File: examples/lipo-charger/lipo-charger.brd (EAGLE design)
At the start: 36 x 12 mm, 10 parts, among them IC2 LIPO_CHARGER/OT

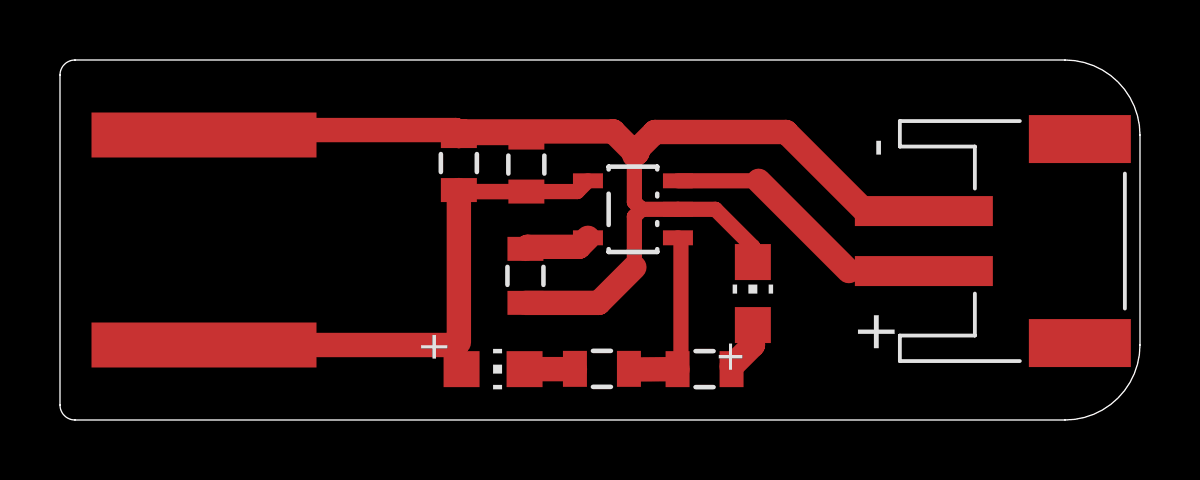
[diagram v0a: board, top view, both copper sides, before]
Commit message: lipo board uses new parts
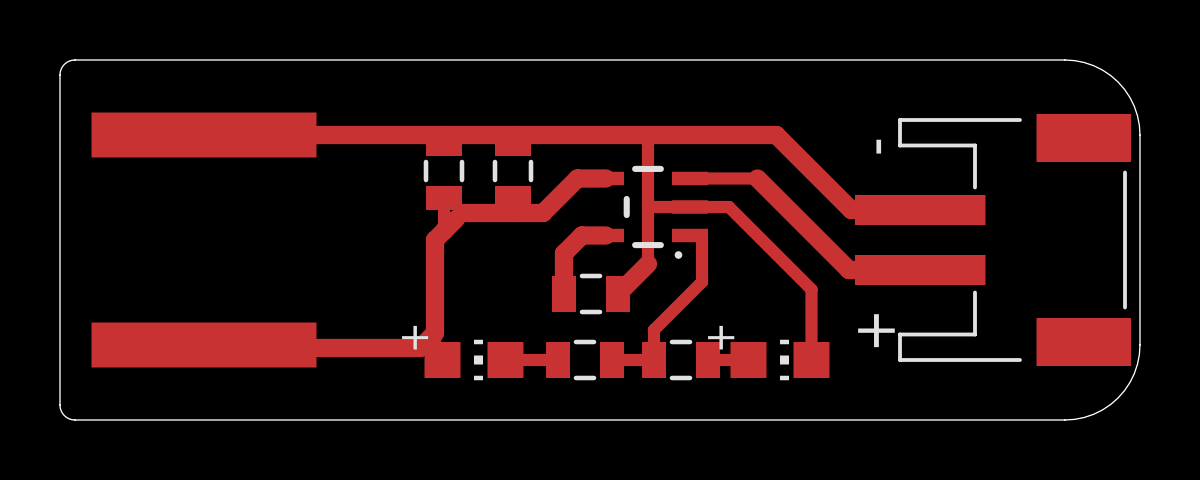
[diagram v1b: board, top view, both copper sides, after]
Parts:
- removed CN1: (no value), homemade-hardware:JST-PH-2-SMT-RA
- removed IC2: LIPO_CHARGER/OT, homemade-hardware:SOT23-5L
- added IC1: IC_LIPO_CHARGER, homemade-hardware:SOT23-5
- added U$1: CONN_BATTERY-LIPO-HORIZ, homemade-hardware:JST-PH-2-SMT-RA
- LED1: value RED-2V/20mA -> Red
- LED2: value GREEN-2V/20mA -> Blue
- R1: value 10k -> 150
- R3: value 150 -> 10k
- U$2: value USB-PCB-POWER -> CONN_USB_PCB_POWER; device homemade-hardware:USB-A-PCB-POWER -> homemade-hardware:USB-PCB-POWER
- moved R3 4.54 mm to (17.7, 4.20)
- moved R1 3.44 mm to (17.5, 2.00), turned to 180 degrees
- moved R2 2.65 mm to (20.7, 2.00)
- moved LED2 2.39 mm to (24.0, 2.00), turned to 270 degrees
- moved LED1 0.70 mm to (13.8, 2.00)
- moved C1 0.56 mm to (12.8, 8.30)
- moved C2 0.49 mm to (15.1, 8.30)
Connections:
- net 5V: now also IC1.4; no longer IC2.4
- net BATTERY: now also IC1.3, U$1.1; no longer CN1.1, IC2.3
- net CURRENT-CONTROL: now also IC1.5, R3.2; no longer IC2.5, R1.2
- net GND: now also IC1.2, R3.1, U$1.2; no longer CN1.2, IC2.2, R1.1
- net N$2: now also R1.2; no longer R2.2
- net N$3: now also R2.1; no longer R3.1
- net STATUS: now also IC1.1, R1.1, R2.2; no longer IC2.1, R2.1, R3.2
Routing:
- net 5V: track 21.3 -> 20.2 mm
- net GND: track 41.2 -> 40.2 mm
- net CURRENT-CONTROL: track 2.24 -> 3.00 mm
- net STATUS: track 6.09 -> 6.61 mm
- net BATTERY: track 9.44 -> 8.94 mm

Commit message: finishes lipo pcb design
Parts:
- moved C1 0.90 mm to (13.7, 8.30)
- moved LED2 0.60 mm to (24.6, 2.00)
- moved C2 0.50 mm to (15.6, 8.30)
- moved R2 0.20 mm to (20.9, 2.00)
- moved R3 0.20 mm to (17.5, 4.20)
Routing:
- net 5V: track 20.2 -> 19.7 mm
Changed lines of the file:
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@@
 <element name="U$2" library="homemade-hardware" package="USB-PCB-POWER" value="CONN_USB_PCB_POWER" x="5" y="6" smashed="yes"/>
 <element name="LED1" library="homemade-hardware" package="CHIP-LED0805" value="Red" x="13.8" y="2" smashed="yes" rot="R270"/>
-<element name="LED2" library="homemade-hardware" package="CHIP-LED0805" value="Blue" x="24" y="2" smashed="yes" rot="R270"/>
-<element name="C1" library="homemade-hardware" package="0805" value="10uF" x="12.8" y="8.3" smashed="yes" rot="R90"/>
-<element name="C2" library="homemade-hardware" package="0805" value="0.1uF" x="15.1" y="8.3" smashed="yes" rot="R90"/>
-<element name="R2" library="homemade-hardware" package="0805" value="150" x="20.7" y="2" smashed="yes" rot="R180"/>
+<element name="LED2" library="homemade-hardware" package="CHIP-LED0805" value="Blue" x="24.6" y="2" smashed="yes" rot="R270"/>
+<element name="C1" library="homemade-hardware" package="0805" value="10uF" x="13.7" y="8.3" smashed="yes" rot="R90"/>
+<element name="C2" library="homemade-hardware" package="0805" value="0.1uF" x="15.6" y="8.3" smashed="yes" rot="R90"/>
+<element name="R2" library="homemade-hardware" package="0805" value="150" x="20.9" y="2" smashed="yes" rot="R180"/>
 <element name="R1" library="homemade-hardware" package="0805" value="150" x="17.5" y="2" smashed="yes" rot="R180"/>
-<element name="R3" library="homemade-hardware" package="0805" value="10k" x="17.7" y="4.2" smashed="yes" rot="R180"/>
+<element name="R3" library="homemade-hardware" package="0805" value="10k" x="17.5" y="4.2" smashed="yes" rot="R180"/>
 </elements>
 <signals>
@@
 <contactref element="IC1" pad="3"/>
 <contactref element="U$1" pad="1"/>
-<wire x1="21.0001" y1="8.05" x2="23.25" y2="8.05" width="0.4064" layer="1"/>
-<wire x1="23.25" y1="8.05" x2="26.3" y2="5" width="0.6096" layer="1"/>
+<wire x1="23.3001" y1="7.95" x2="23.2001" y2="8.05" width="0.4064" layer="1"/>
+<wire x1="21.0001" y1="8.05" x2="23.2001" y2="8.05" width="0.4064" layer="1"/>
+<wire x1="23.35" y1="7.95" x2="23.3001" y2="7.95" width="0.4064" layer="1"/>
+<wire x1="23.35" y1="7.95" x2="26.3" y2="5" width="0.6096" layer="1"/>
 <wire x1="26.3" y1="5" x2="28.675" y2="5" width="0.6096" layer="1"/>
 </signal>
@@
 <contactref element="IC1" pad="5"/>
 <contactref element="R3" pad="2"/>
-<wire x1="16.8" y1="4.2" x2="16.8" y2="5.5501" width="0.6096" layer="1"/>
-<wire x1="17.3999" y1="6.15" x2="16.8" y2="5.5501" width="0.6096" layer="1"/>
-<wire x1="17.3999" y1="6.15" x2="18.1999" y2="6.15" width="0.6096" layer="1"/>
+<wire x1="16.6" y1="4.2" x2="16.6" y2="5.1501" width="0.6096" layer="1"/>
+<wire x1="17.5999" y1="6.15" x2="16.6" y2="5.1501" width="0.6096" layer="1"/>
+<wire x1="17.5999" y1="6.15" x2="18.1999" y2="6.15" width="0.6096" layer="1"/>
 </signal>
 <signal name="STATUS">
@@
 <contactref element="R1" pad="1"/>
 <contactref element="R2" pad="2"/>
-<wire x1="19.8" y1="2" x2="18.4" y2="2" width="0.4064" layer="1"/>
+<wire x1="20" y1="2" x2="18.4" y2="2" width="0.4064" layer="1"/>
 <wire x1="21.0001" y1="6.15" x2="21.4001" y2="6.15" width="0.4064" layer="1"/>
-<wire x1="21.4001" y1="6.15" x2="21.4001" y2="4.6001" width="0.4064" layer="1"/>
-<wire x1="21.4001" y1="4.6001" x2="19.8" y2="3" width="0.4064" layer="1"/>
-<wire x1="19.8" y1="3" x2="19.8" y2="2" width="0.4064" layer="1"/>
+<wire x1="21.4001" y1="6.15" x2="21.4001" y2="4.4001" width="0.4064" layer="1"/>
+<wire x1="21.4001" y1="4.4001" x2="20" y2="3" width="0.6096" layer="1"/>
+<wire x1="20" y1="3" x2="20" y2="2" width="0.6096" layer="1"/>
 </signal>
 <signal name="5V">
@@
 <contactref element="C1" pad="1"/>
 <contactref element="C2" pad="1"/>
-<wire x1="18.1999" y1="8.05" x2="17.25" y2="8.05" width="0.6096" layer="1"/>
-<wire x1="17.25" y1="8.05" x2="16.1" y2="6.9" width="0.6096" layer="1"/>
-<wire x1="16.1" y1="6.9" x2="15.1" y2="6.9" width="0.6096" layer="1"/>
-<wire x1="15.1" y1="6.9" x2="13.4" y2="6.9" width="0.6096" layer="1"/>
-<wire x1="13.4" y1="6.9" x2="13.2" y2="6.7" width="0.4064" layer="1"/>
-<wire x1="13.2" y1="6.7" x2="12.8" y2="6.3" width="0.6096" layer="1"/>
-<wire x1="12.8" y1="6.3" x2="12.5" y2="6" width="0.6096" layer="1"/>
-<wire x1="12.5" y1="2.9" x2="12" y2="2.4" width="0.6096" layer="1"/>
-<wire x1="12" y1="2.4" x2="4.9" y2="2.4" width="0.6096" layer="1"/>
-<wire x1="4.9" y1="2.4" x2="4.8" y2="2.5" width="0.8128" layer="1"/>
-<wire x1="12.5" y1="6" x2="12.5" y2="2.9" width="0.6096" layer="1"/>
-<wire x1="15.1" y1="6.9" x2="15.1" y2="7.4" width="0.4064" layer="1"/>
-<wire x1="12.8" y1="7.4" x2="12.8" y2="6.3" width="0.4064" layer="1"/>
+<wire x1="18.1999" y1="8.05" x2="17.35" y2="8.05" width="0.6096" layer="1"/>
+<wire x1="17.35" y1="8.05" x2="16.2" y2="6.9" width="0.6096" layer="1"/>
+<wire x1="16.2" y1="6.9" x2="15.6" y2="6.9" width="0.6096" layer="1"/>
+<wire x1="15.6" y1="6.9" x2="14.7" y2="6.9" width="0.6096" layer="1"/>
+<wire x1="14.7" y1="6.9" x2="14.1" y2="6.3" width="0.6096" layer="1"/>
+<wire x1="14.1" y1="6.3" x2="13.9" y2="6.1" width="0.6096" layer="1"/>
+<wire x1="14.1" y1="7.4" x2="14.1" y2="6.3" width="0.4064" layer="1"/>
+<wire x1="13.9" y1="6.1" x2="13.9" y2="5.9" width="0.4064" layer="1"/>
+<wire x1="13.9" y1="5.9" x2="13.9" y2="3.8" width="0.6096" layer="1"/>
+<wire x1="13.9" y1="3.8" x2="12.5" y2="2.4" width="0.6096" layer="1"/>
+<wire x1="13.7" y1="7.4" x2="14.1" y2="7.4" width="0.6096" layer="1"/>
+<wire x1="12.5" y1="2.5" x2="4.8" y2="2.5" width="0.6096" layer="1"/>
+<wire x1="15.6" y1="6.9" x2="15.6" y2="7.4" width="0.4064" layer="1"/>
 <wire x1="12.75" y1="2" x2="12.5" y2="2.25" width="0.6096" layer="1"/>
-<wire x1="12.5" y1="2.25" x2="12.5" y2="2.9" width="0.4064" layer="1"/>
+<wire x1="12.5" y1="2.25" x2="12.5" y2="2.4" width="0.4064" layer="1"/>
+<wire x1="12.5" y1="2.4" x2="12.5" y2="2.5" width="0.4064" layer="1"/>
 </signal>
 <signal name="N$2">
@@
 <contactref element="R2" pad="1"/>
 <contactref element="LED2" pad="A"/>
-<wire x1="21.6" y1="2" x2="22.95" y2="2" width="0.4064" layer="1"/>
+<wire x1="21.8" y1="2" x2="23.55" y2="2" width="0.4064" layer="1"/>
 </signal>
 <signal name="GND">
-<contactref element="U$1" pad="2"/>
-<contactref element="IC1" pad="2"/>
 <contactref element="U$2" pad="GND"/>
-<contactref element="R3" pad="1"/>
 <contactref element="LED2" pad="C"/>
 <contactref element="C1" pad="2"/>
 <contactref element="C2" pad="2"/>
-<wire x1="4.8" y1="9.5" x2="12.8" y2="9.5" width="0.6096" layer="1"/>
-<wire x1="12.8" y1="9.5" x2="15.1" y2="9.5" width="0.6096" layer="1"/>
-<wire x1="15.1" y1="9.5" x2="19.6" y2="9.5" width="0.6096" layer="1"/>
+<contactref element="IC1" pad="2"/>
+<contactref element="R3" pad="1"/>
+<wire x1="25.65" y1="3.55" x2="22.2" y2="7" width="0.6096" layer="1"/>
+<wire x1="22.2" y1="7" x2="22.1001" y2="7" width="0.4064" layer="1"/>
+<wire x1="22.1001" y1="7" x2="22.0001" y2="7.1" width="0.4064" layer="1"/>
+<wire x1="22.0001" y1="7.1" x2="21.0001" y2="7.1" width="0.4064" layer="1"/>
+<contactref element="U$1" pad="2"/>
 <wire x1="19.6" y1="9.5" x2="23.875" y2="9.5" width="0.6096" layer="1"/>
 <wire x1="26.375" y1="7" x2="23.875" y2="9.5" width="0.6096" layer="1"/>
 <wire x1="26.375" y1="7" x2="28.675" y2="7" width="0.6096" layer="1"/>
-<wire x1="18.6" y1="4.2" x2="19.6" y2="5.2" width="0.6096" layer="1"/>
 <wire x1="19.6" y1="5.2" x2="19.6" y2="7.1" width="0.4064" layer="1"/>
 <wire x1="19.6" y1="7.1" x2="19.6" y2="9.5" width="0.4064" layer="1"/>
-<wire x1="12.8" y1="9.2" x2="12.8" y2="9.5" width="0.4064" layer="1"/>
-<wire x1="15.1" y1="9.2" x2="15.1" y2="9.5" width="0.4064" layer="1"/>
-<wire x1="25.05" y1="2" x2="25.05" y2="4.35" width="0.4064" layer="1"/>
-<wire x1="25.05" y1="4.35" x2="22.3" y2="7.1" width="0.4064" layer="1"/>
-<wire x1="22.3" y1="7.1" x2="21.0001" y2="7.1" width="0.4064" layer="1"/>
+<wire x1="4.8" y1="9.5" x2="13.7" y2="9.5" width="0.6096" layer="1"/>
+<wire x1="13.7" y1="9.5" x2="15.6" y2="9.5" width="0.6096" layer="1"/>
+<wire x1="15.6" y1="9.5" x2="19.6" y2="9.5" width="0.6096" layer="1"/>
+<wire x1="18.4" y1="4.2" x2="18.85020625" y2="4.2" width="0.6096" layer="1"/>
+<wire x1="18.85020625" y1="4.2" x2="19.6" y2="4.94979375" width="0.6096" layer="1"/>
+<wire x1="19.6" y1="4.94979375" x2="19.6" y2="5.2" width="0.6096" layer="1"/>
 <wire x1="21.0001" y1="7.1" x2="19.6" y2="7.1" width="0.4064" layer="1"/>
+<wire x1="15.6" y1="9.2" x2="15.6" y2="9.5" width="0.4064" layer="1"/>
+<wire x1="13.7" y1="9.2" x2="13.7" y2="9.5" width="0.4064" layer="1"/>
+<wire x1="25.65" y1="2" x2="25.65" y2="3.55" width="0.6096" layer="1"/>
 </signal>
 </signals>
